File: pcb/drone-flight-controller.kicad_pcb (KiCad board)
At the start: 4 copper layers, 102 x 49 mm, 160 parts, among them J1 SWD, J10 CONN_MANDO, J11 OLED, J12 STM32 SPI, J13 STM32 I2C, J14 STM32 USART, J15 ICSP, J16 USB_B_Micro, J17 Conn_Coaxial, J2 Jumper, J3 USB_B_Micro, J4 CONN_MOT_1, J5 CONN_MOT_2, J6 CONN_MOT_3, J7 CONN_MOT_4, J8 XT-60, J9 LIDAR, SW1 TC-6610_C7528713, SW2 TC-6610_C7528713, SW3 TC-6610_C7528713, SW4 SS12D10G5_C7431054, U1 STM32F103R8T6, U10 LM7805_TO220, U11 AMS1117-3.3, U2 MPU-6050, U3 ATMEGA328P-AU, U4 CH340G, U5 LM358DR, U6 74HC245, U7 nRF24L01P, U8 MICROSD_C164170, U9 74AHC1G125, Y1 8MHz, Y2 32.768KHz, Y3 16MHz, Y4 12MHz, Y5 16MHz

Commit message: pcb: F8 sync - TS-1088 SMD footprints replace the THT tacts on the board
Includes in-progress hand placement from the same session (switch row at
y=113.7, U8 reposition, silk font normalization). Board is mid-placement,
unrouted: DRC noise is ratsnest + silk/text-height artifacts, none of it
involves the swapped switches.
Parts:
- SW1, SW2, SW3: value TC-6610_C7528713 -> TS-1088-AR02016_C720477; footprint Button_Switch_THT:SW_PUSH_6mm_H9.5mm -> easyeda:SW-SMD_L3.9-W3.0-P4.45
- moved U5 392.8 mm to (367.7, 150.5)
- moved C6 241.9 mm to (123.5, 95.6), turned to 90 degrees
- moved C4 240.5 mm to (124.7, 95.6), turned to 90 degrees
- moved C10 240.4 mm to (128.2, 85.1), turned to 180 degrees
- moved C5 239.2 mm to (126.1, 94.5), turned to -90 degrees
- moved C2 237.1 mm to (127.8, 108.1), turned to 180 degrees
- moved C45 230.7 mm to (97.4, 81.5), turned to 180 degrees
- moved C46 229.2 mm to (99.4, 81.5)
- moved C3 229.2 mm to (135.6, 107.0), turned to -90 degrees
- moved C1 228.2 mm to (136.8, 95.6), turned to 90 degrees
- moved C47 224.7 mm to (100.2, 98.2), turned to 180 degrees
- moved Y1 220.0 mm to (121.4, 100.3), turned to -90 degrees
- moved C23 217.0 mm to (98.3, 103.6), turned to -90 degrees
- moved C21 215.1 mm to (99.4, 103.6), turned to -90 degrees
- moved C33 213.9 mm to (107.2, 95.9)
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
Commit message: provisional final component placements
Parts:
- SW4: value SS12D10G5_C7431054 -> K3-1204D_C145861; footprint easyeda:SW-TH_SHOU-HAN_SS12D10G4 -> easyeda:SW-TH_K3-1204D
- moved R39 254.5 mm to (94.0, 72.8), turned to 90 degrees
- moved C11 249.8 mm to (118.0, 100.4), turned to 90 degrees
- moved C12 249.7 mm to (118.0, 105.1), turned to -90 degrees
- moved C13 248.4 mm to (119.8, 96.3), turned to 90 degrees
- moved C14 248.4 mm to (119.8, 98.3), turned to 90 degrees
- moved C9 248.1 mm to (119.6, 111.7), turned to -90 degrees
- moved U5 248.0 mm to (136.1, 61.9)
- moved C8 245.3 mm to (122.4, 107.2), turned to -90 degrees
- moved C19 245.0 mm to (125.6, 110.1)
- moved C7 243.7 mm to (121.3, 107.3), turned to -90 degrees
- moved D14 243.3 mm to (95.7, 72.8), turned to -90 degrees
- moved D1 239.6 mm to (130.3, 82.4), turned to -90 degrees
- moved Y2 239.0 mm to (121.6, 97.3), turned to 90 degrees
- moved Y5 236.0 mm to (116.9, 76.7), turned to -90 degrees
- moved R36 234.8 mm to (107.8, 74.3), turned to -90 degrees
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
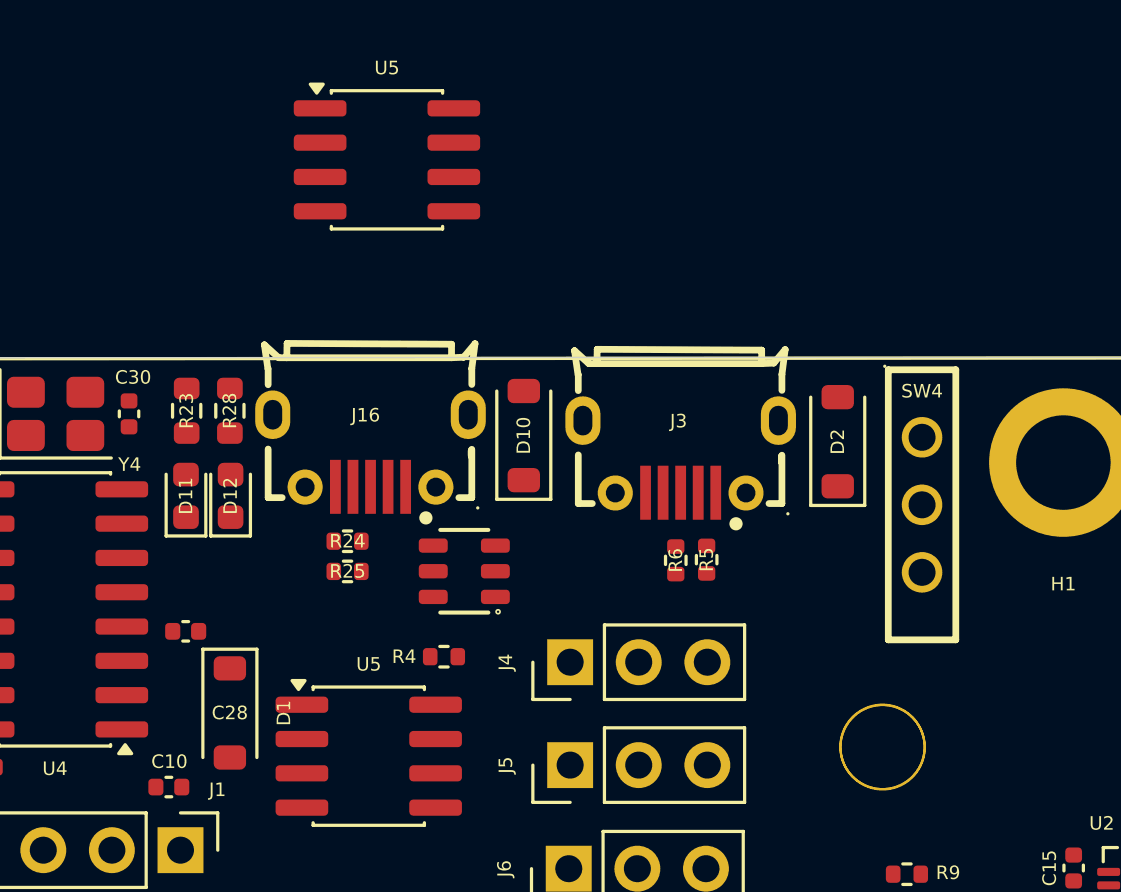
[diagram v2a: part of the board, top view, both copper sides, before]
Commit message: copper zones and JPI logo
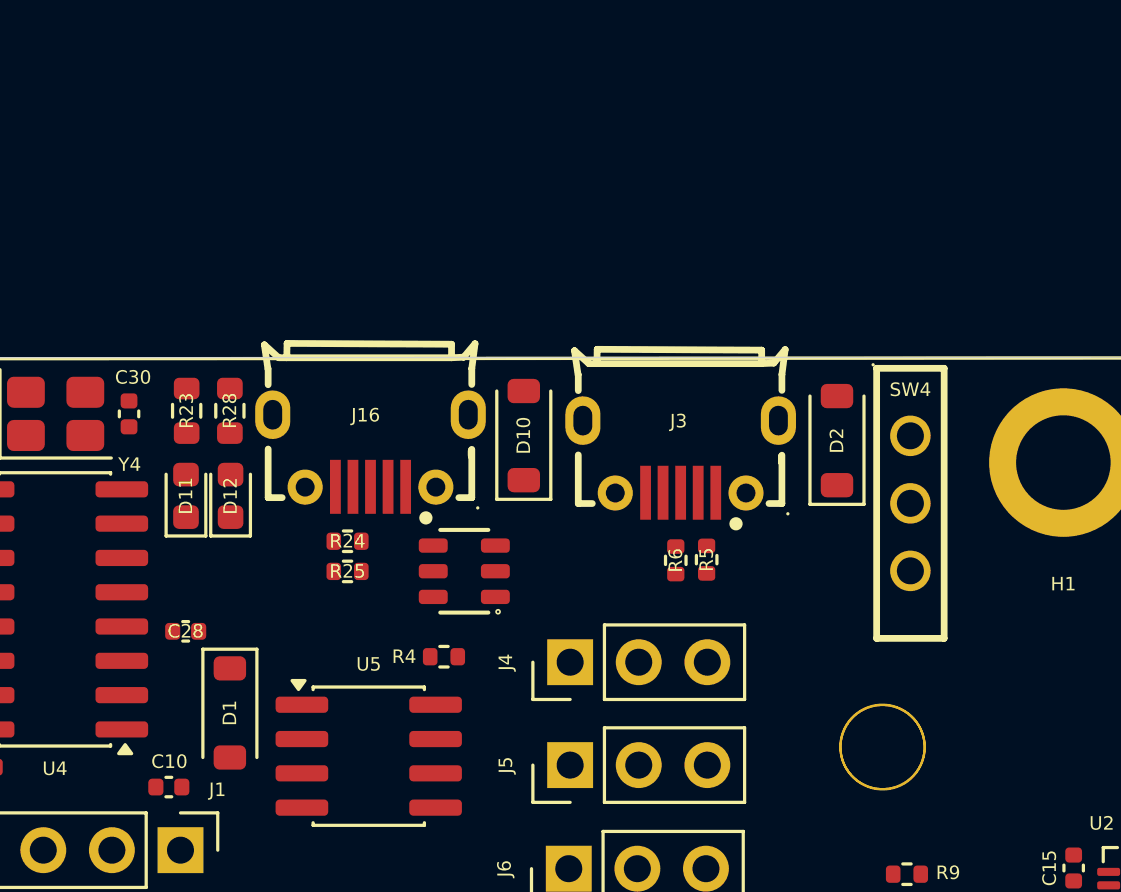
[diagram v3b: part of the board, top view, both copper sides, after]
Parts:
- removed the U5 at (136.1, 61.9)
- moved SW4 0.44 mm to (155.5, 74.6)
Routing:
- added copper zone on In2.Cu, net (none)
- added copper zone on In2.Cu, net +12V
- added copper zone on In2.Cu, net +3.3V
- added copper zone on In1.Cu, net GND
- added copper zone on In2.Cu, net Vdrive
